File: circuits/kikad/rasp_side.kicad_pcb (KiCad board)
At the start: 2 copper layers, 33 parts, among them J1 RJ45, J2 RJ45, J3 RJ45, J4 RJ45, P1 CONN_13X2

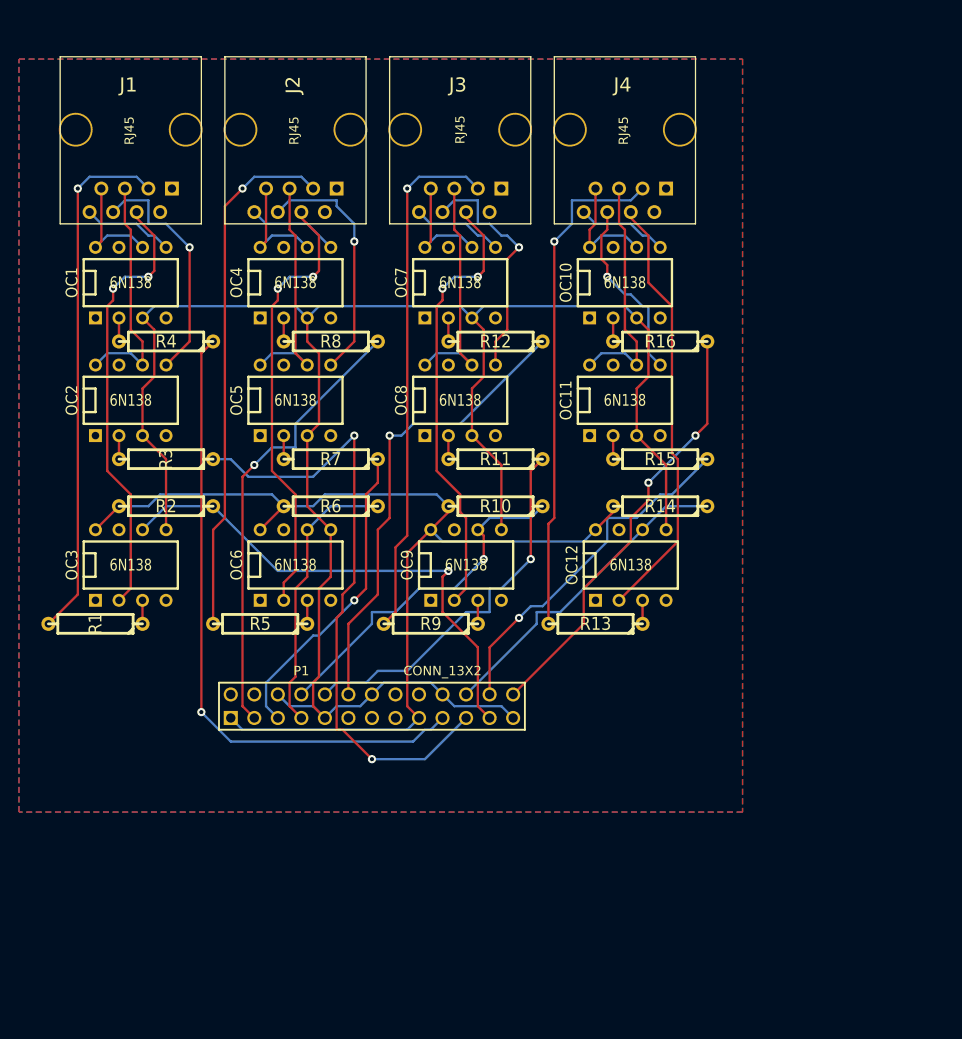
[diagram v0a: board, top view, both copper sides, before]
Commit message: improved version of the kicad circuit
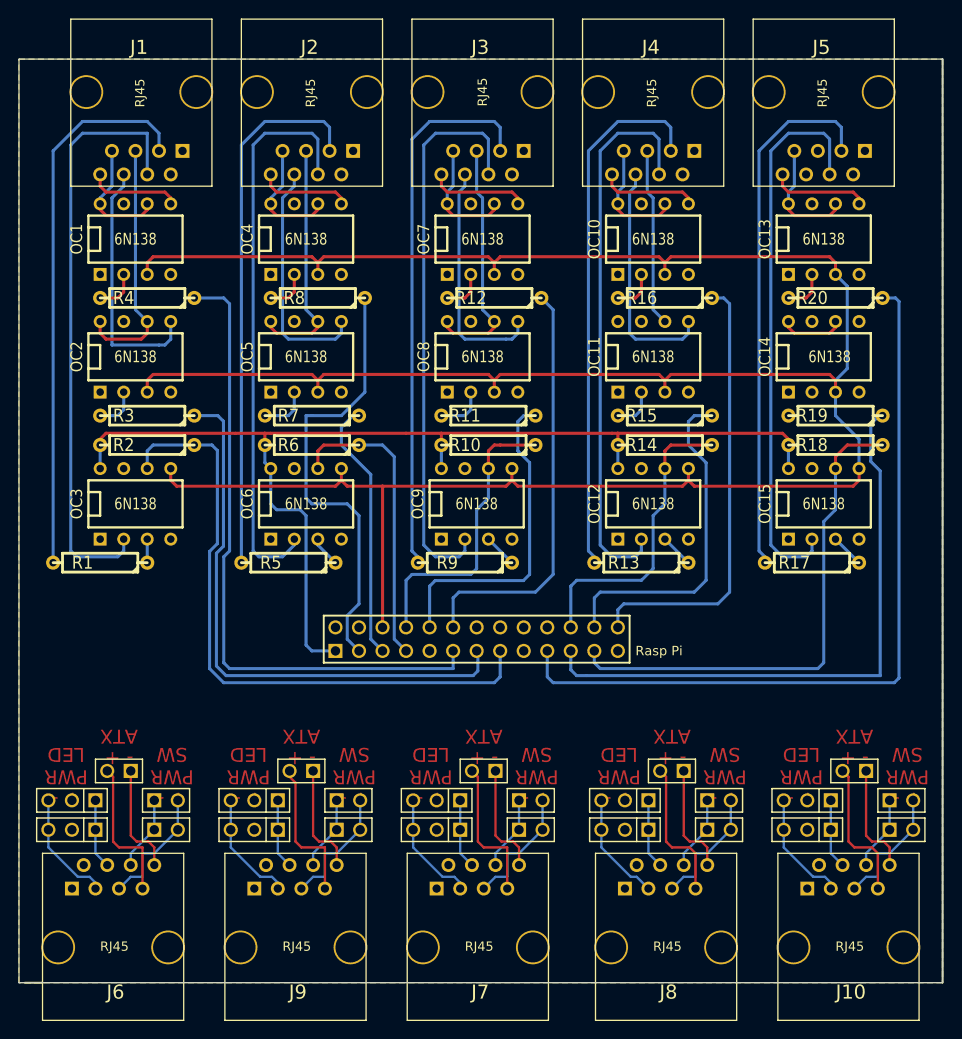
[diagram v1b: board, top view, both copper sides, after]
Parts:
- removed P1: CONN_13X2, pin_array_13x2
- added ?: , PIN_ARRAY_3X1, F.Cu at (95.2, 93.3)
- added ?: , PIN_ARRAY_3X1, F.Cu at (15.9, 90.2)
- added ?: , PIN_ARRAY_2X1, F.Cu at (100.3, 87.0)
- added ?: , PIN_ARRAY_2X1, F.Cu at (105.4, 93.3)
- added ?: , PIN_ARRAY_2X1, F.Cu at (40.6, 87.0)
- added ?: , PIN_ARRAY_2X1, F.Cu at (45.7, 93.3)
- added ?: , PIN_ARRAY_2X1, F.Cu at (45.7, 90.2)
- added ?: , PIN_ARRAY_2X1, F.Cu at (105.4, 90.2)
- added ?: , PIN_ARRAY_2X1, F.Cu at (80.6, 87.0)
- added ?: , PIN_ARRAY_2X1, F.Cu at (85.7, 93.3)
- added ?: , PIN_ARRAY_2X1, F.Cu at (85.7, 90.2)
- added ?: , PIN_ARRAY_3X1, F.Cu at (35.6, 93.3)
- added ?: , PIN_ARRAY_2X1, F.Cu at (60.3, 87.0)
- added ?: , PIN_ARRAY_2X1, F.Cu at (65.4, 93.3)
- added ?: , PIN_ARRAY_2X1, F.Cu at (65.4, 90.2)
- added ?: , PIN_ARRAY_2X1, F.Cu at (21.0, 87.0)
- added ?: , PIN_ARRAY_2X1, F.Cu at (26.0, 90.2)
- added ?: , PIN_ARRAY_2X1, F.Cu at (26.0, 93.3)
- added ?: , PIN_ARRAY_3X1, F.Cu at (35.6, 90.2)
- added ?: , PIN_ARRAY_3X1, F.Cu at (75.6, 93.3)
- added ?: , PIN_ARRAY_3X1, F.Cu at (75.6, 90.2)
- added ?: , PIN_ARRAY_3X1, F.Cu at (95.2, 90.2)
- added ?: , PIN_ARRAY_3X1, F.Cu at (55.2, 93.3)
- added ?: , PIN_ARRAY_3X1, F.Cu at (55.2, 90.2)
- added ?: , PIN_ARRAY_3X1, F.Cu at (15.9, 93.3)
- added J10: RJ45, RJ45_8, F.Cu at (99.7, 106.0)
- added J5: RJ45, RJ45_8, F.Cu at (97.0, 13.7)
- added J6: RJ45, RJ45_8, F.Cu at (20.3, 106.0)
- added J7: RJ45, RJ45_8, F.Cu at (59.7, 106.0)
- added J8: RJ45, RJ45_8, F.Cu at (80.0, 106.0)
- added J9: RJ45, RJ45_8, F.Cu at (40.0, 106.0)
- added OC13: 6N138, DIP-8__300, F.Cu at (97.0, 29.6)
- added OC14: 6N138, DIP-8__300, F.Cu at (97.0, 42.3)
- added OC15: 6N138, DIP-8__300, F.Cu at (97.0, 58.2)
- added R17: 4k, R4, F.Cu at (95.8, 64.5)
- added R18: 10k, R4, F.Cu at (98.3, 51.8)
- added R19: 1.2k, R4, F.Cu at (98.3, 48.6)
- added R20: 1.2k, R4, F.Cu at (98.3, 35.9)
- added Rasp Pi: , pin_array_13x2, F.Cu at (59.6, 72.8)
- moved R13 8.26 mm to (77.3, 64.5)
- moved R9 7.56 mm to (58.3, 64.5)
- moved R5 7.27 mm to (39.2, 64.5)
- moved OC12 7.03 mm to (78.6, 58.2)
- moved R2 6.91 mm to (24.0, 51.8)
- moved R6 6.91 mm to (41.8, 51.8)
- moved OC6 6.70 mm to (41.1, 58.2)
- moved OC9 6.70 mm to (59.6, 58.2)
- moved R10 6.65 mm to (60.8, 51.8)
- moved OC3 6.62 mm to (22.7, 58.2)
- moved R1 6.62 mm to (18.9, 64.5)
- moved R14 6.62 mm to (79.9, 51.8)
- moved OC11 5.60 mm to (78.6, 42.3)
- moved OC10 5.60 mm to (78.6, 29.6)
- moved OC8 5.28 mm to (60.2, 42.3)
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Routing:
- net N-0000020: track 0.00 -> 83.8 mm
- net GND: track 208.1 -> 286.5 mm
- net N-0000021: track 0.00 -> 64.9 mm
- net N-000005: track 0.00 -> 60.3 mm
- net N-000001: track 0.00 -> 57.7 mm
- net N-0000018: track 0.00 -> 54.9 mm
- net N-0000092: track 47.9 -> 64.6 mm, vias 2 -> 0
- net N-0000074: track 0.00 -> 15.8 mm
- net N-0000010: track 0.00 -> 15.8 mm
- net N-0000046: track 0.00 -> 15.8 mm
- net N-0000079: track 0.00 -> 15.4 mm
- net N-0000057: track 0.00 -> 15.4 mm
- net N-0000094: track 55.2 -> 68.9 mm, vias 1 -> 0
- net N-0000066: track 0.00 -> 13.6 mm
- net N-0000082: track 0.00 -> 13.6 mm
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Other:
- board outline added: 99.7 x 99.7 mm
- net class Default: clearance 0.254 -> 0.3302; trace_width 0.254 -> 0.3302
- rule trace_clearance: 0.254 -> 0.3302
- board text added: "+ - PWR LED"
- board text added: "+ - PWR SW"
- board text added: "- + ATX"

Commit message: update the circuit a little
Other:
- board text added: "3.3"
- board text added: "A1"
- board text added: "A2"
- board text added: "A3"
- board text added: "GND"
- board text added: "L1"
- board text added: "L2"
- board text added: "L3"
- board text added: "MùPùF, 2014"
- board text added: "P1"
- board text added: "P2"
- board text added: "P3"
- board text added: "Rasp/Wt-RPM 2014, MùPùF"
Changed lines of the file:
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@@
     (links 151)
     (no_connects 5)
-    (area 10.109999 5.702299 109.955001 114.312701)
+    (area 10.059999 5.448299 109.955001 114.312701)
     (thickness 1.6)
-    (drawings 21)
+    (drawings 60)
     (tracks 599)
     (zones 0)
@@
     )
   )
+  (gr_text A3 (at 57.15 68.326 90) (layer F.SilkS)
+    (effects (font (size 1.5 1.5) (thickness 0.3)))
+  )
+  (gr_text P3 (at 54.61 68.326 90) (layer F.SilkS)
+    (effects (font (size 1.5 1.5) (thickness 0.3)))
+  )
+  (gr_text L3 (at 52.07 68.326 90) (layer F.SilkS)
+    (effects (font (size 1.5 1.5) (thickness 0.3)))
+  )
+  (gr_text L2 (at 52.07 76.962 90) (layer F.SilkS)
+    (effects (font (size 1.5 1.5) (thickness 0.3)))
+  )
+  (gr_text P2 (at 49.53 76.962 90) (layer F.SilkS)
+    (effects (font (size 1.5 1.5) (thickness 0.3)))
+  )
+  (gr_text A2 (at 46.736 76.962 90) (layer F.SilkS)
+    (effects (font (size 1.5 1.5) (thickness 0.3)))
+  )
+  (gr_text L1 (at 62.23 76.708 90) (layer F.SilkS)
+    (effects (font (size 1.5 1.5) (thickness 0.3)))
+  )
+  (gr_text P1 (at 59.69 76.708 90) (layer F.SilkS)
+    (effects (font (size 1.5 1.5) (thickness 0.3)))
+  )
+  (gr_text A1 (at 57.15 76.708 90) (layer F.SilkS)
+    (effects (font (size 1.5 1.5) (thickness 0.3)))
+  )
+  (gr_line (start 89.916 109.728) (end 89.916 80.01) (angle 90) (layer B.SilkS) (width 0.2))
+  (gr_line (start 69.85 109.728) (end 69.85 80.01) (angle 90) (layer B.SilkS) (width 0.2))
+  (gr_line (start 50.038 80.01) (end 50.292 80.264) (angle 90) (layer B.SilkS) (width 0.2))
+  (gr_line (start 50.038 109.982) (end 50.038 80.01) (angle 90) (layer B.SilkS) (width 0.2))
+  (gr_line (start 30.226 80.01) (end 30.226 108.458) (angle 90) (layer B.SilkS) (width 0.2))
+  (gr_line (start 30.226 109.728) (end 30.226 80.01) (angle 90) (layer B.SilkS) (width 0.2))
+  (gr_text "MùPùF, 2014" (at 100.076 83.566 180) (layer B.SilkS)
+    (effects (font (size 1.5 1.5) (thickness 0.3)) (justify mirror))
+  )
+  (gr_text "MùPùF, 2014" (at 80.518 83.566 180) (layer B.SilkS)
+    (effects (font (size 1.5 1.5) (thickness 0.3)) (justify mirror))
+  )
+  (gr_text "MùPùF, 2014" (at 60.198 83.82 180) (layer B.SilkS)
+    (effects (font (size 1.5 1.5) (thickness 0.3)) (justify mirror))
+  )
+  (gr_text "MùPùF, 2014" (at 40.64 83.82 180) (layer B.SilkS)
+    (effects (font (size 1.5 1.5) (thickness 0.3)) (justify mirror))
+  )
+  (gr_text "- +\nATX" (at 20.955 84.455 180) (layer F.Cu)
+    (effects (font (size 1.5 1.5) (thickness 0.3)))
+  )
+  (gr_text "MùPùF, 2014" (at 21.082 83.82 180) (layer B.SilkS)
+    (effects (font (size 1.5 1.5) (thickness 0.3)) (justify mirror))
+  )
+  (gr_text "MùPùF, 2014" (at 21.082 83.82 180) (layer B.SilkS)
+    (effects (font (size 1.5 1.5) (thickness 0.3)) (justify mirror))
+  )
+  (gr_text "- +\nATX" (at 20.955 84.455 180) (layer F.Cu)
+    (effects (font (size 1.5 1.5) (thickness 0.3)))
+  )
+  (gr_text "- +\nATX" (at 20.955 84.455 180) (layer F.Cu)
+    (effects (font (size 1.5 1.5) (thickness 0.3)))
+  )
+  (gr_text "MùPùF, 2014" (at 21.082 83.82 180) (layer B.SilkS)
+    (effects (font (size 1.5 1.5) (thickness 0.3)) (justify mirror))
+  )
+  (gr_text "MùPùF, 2014" (at 21.082 83.82 180) (layer B.SilkS)
+    (effects (font (size 1.5 1.5) (thickness 0.3)) (justify mirror))
+  )
+  (gr_text "Rasp/Wt-RPM\n\n2014, MùPùF" (at 19.812 71.374) (layer F.SilkS)
+    (effects (font (size 1.5 1.5) (thickness 0.3)))
+  )
+  (gr_text GND (at 49.53 67.564 90) (layer F.SilkS)
+    (effects (font (size 1.5 1.5) (thickness 0.3)))
+  )
+  (gr_text 3.3 (at 44.45 77.216 90) (layer F.SilkS)
+    (effects (font (size 1.5 1.5) (thickness 0.3)))
+  )
+  (gr_line (start 10.668 80.01) (end 109.728 80.01) (angle 90) (layer F.SilkS) (width 0.2))
+  (gr_line (start 89.916 80.01) (end 89.916 109.728) (angle 90) (layer F.Paste) (width 0.2))
+  (gr_line (start 69.85 109.728) (end 69.85 108.712) (angle 90) (layer F.Paste) (width 0.2))
+  (gr_line (start 69.85 80.01) (end 69.85 109.728) (angle 90) (layer F.Paste) (width 0.2))
+  (gr_line (start 50.038 80.01) (end 50.038 109.728) (angle 90) (layer F.Paste) (width 0.2))
+  (gr_line (start 30.226 80.264) (end 30.226 109.982) (angle 90) (layer F.Paste) (width 0.2))
+  (gr_line (start 30.48 109.728) (end 30.48 109.474) (angle 90) (layer F.Paste) (width 0.2))
+  (gr_line (start 10.16 80.01) (end 11.938 80.01) (angle 90) (layer F.Paste) (width 0.2))
+  (gr_line (start 109.474 80.01) (end 109.728 80.01) (angle 90) (layer F.Paste) (width 0.2))
+  (gr_line (start 11.938 80.01) (end 109.474 80.01) (angle 90) (layer F.Paste) (width 0.2))
   (gr_text "- +\nATX" (at 100.33 84.455 180) (layer F.Cu)
     (effects (font (size 1.5 1.5) (thickness 0.3)))
@@
     (effects (font (size 1.5 1.5) (thickness 0.3)))
   )
-  (gr_text "+ -\nPWR\nSW" (at 26.67 87.63 180) (layer F.Cu)
+  (gr_text "+ -\nPWR\nSW" (at 26.162 88.138 180) (layer F.Cu)
     (effects (font (size 1.5 1.5) (thickness 0.3)))
   )

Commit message: kicad: add holes in the circuit
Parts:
- added ?: , 1pin, F.Cu at (15.2, 74.4)
- added ?: , 1pin, F.Cu at (104.6, 75.9)
- added ?: , 1pin, F.Cu at (105.9, 29.7)
- added ?: , small_hole, F.Cu at (13.0, 81.5)
- added ?: , small_hole, F.Cu at (27.9, 81.5)
- added ?: , small_hole, F.Cu at (32.5, 81.5)
- added ?: , small_hole, F.Cu at (48.0, 81.5)
- added ?: , small_hole, F.Cu at (52.3, 81.5)
- added ?: , small_hole, F.Cu at (68.1, 81.5)
- added ?: , small_hole, F.Cu at (72.6, 81.5)
- added ?: , small_hole, F.Cu at (88.1, 81.5)
- added ?: , small_hole, F.Cu at (92.7, 81.5)
- added ?: , small_hole, F.Cu at (107.4, 81.5)
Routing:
- net N-000003: track 0.00 -> 25.6 mm
- net +3.3V: track 118.4 -> 140.8 mm
- net N-000004: track 6.88 -> 26.1 mm
- net N-0000032: track 19.2 -> 25.4 mm
- net GND: track 286.5 -> 291.9 mm
- net N-000008: track 0.00 -> 4.48 mm
- net N-0000021: track 64.9 -> 63.2 mm
- net N-0000018: track 54.9 -> 53.4 mm
- net N-0000020: track 83.8 -> 83.0 mm
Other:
- board text added: "A4"
- board text added: "A5"
- board text added: "L = PW LED P = PW SW A = ATX SW"
- board text added: "L4"
- board text added: "L5"
- board text added: "P4"
- board text added: "P5"
- board text added: "Wt-RPM 2014, MùPùF"
- board text removed: "Rasp/Wt-RPM 2014, MùPùF"

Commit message: kicad: style fixes
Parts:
- moved ? 0.25 mm to (13.0, 81.8)
- moved ? 0.25 mm to (27.9, 81.8)
- moved ? 0.25 mm to (32.5, 81.8)
- moved ? 0.25 mm to (48.0, 81.8)
- moved ? 0.25 mm to (52.3, 81.8)
- moved ? 0.25 mm to (68.1, 81.8)
- moved ? 0.25 mm to (72.6, 81.8)
- moved ? 0.25 mm to (88.1, 81.8)
- moved ? 0.25 mm to (92.7, 81.8)
- moved ? 0.25 mm to (107.4, 81.8)
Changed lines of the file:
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@@
     (area 10.059999 5.448299 109.955001 114.312701)
     (thickness 1.6)
-    (drawings 74)
+    (drawings 67)
     (tracks 638)
     (zones 0)
@@
   )
   (module small_hole (layer F.Cu)
-    (at 12.954 81.534)
+    (at 12.954 81.788)
     (descr "module 1 pin (ou trou mecanique de percage)")
     (tags DEV)
@@
   )
   (module small_hole (layer F.Cu)
-    (at 27.94 81.534)
+    (at 27.94 81.788)
     (descr "module 1 pin (ou trou mecanique de percage)")
     (tags DEV)
@@
   )
   (module small_hole (layer F.Cu)
-    (at 32.512 81.534)
+    (at 32.512 81.788)
     (descr "module 1 pin (ou trou mecanique de percage)")
     (tags DEV)
@@
   )
   (module small_hole (layer F.Cu)
-    (at 48.006 81.534)
+    (at 48.006 81.788)
     (descr "module 1 pin (ou trou mecanique de percage)")
     (tags DEV)
@@
   )
   (module small_hole (layer F.Cu)
-    (at 52.324 81.534)
+    (at 52.324 81.788)
     (descr "module 1 pin (ou trou mecanique de percage)")
     (tags DEV)
@@
   )
   (module small_hole (layer F.Cu)
-    (at 68.072 81.534)
+    (at 68.072 81.788)
     (descr "module 1 pin (ou trou mecanique de percage)")
     (tags DEV)
@@
   )
   (module small_hole (layer F.Cu)
-    (at 72.644 81.534)
+    (at 72.644 81.788)
     (descr "module 1 pin (ou trou mecanique de percage)")
     (tags DEV)
@@
   )
   (module small_hole (layer F.Cu)
-    (at 88.138 81.534)
+    (at 88.138 81.788)
     (descr "module 1 pin (ou trou mecanique de percage)")
     (tags DEV)
@@
   )
   (module small_hole (layer F.Cu)
-    (at 92.71 81.534)
+    (at 92.71 81.788)
     (descr "module 1 pin (ou trou mecanique de percage)")
     (tags DEV)
@@
   )
   (module small_hole (layer F.Cu)
-    (at 107.442 81.534)
+    (at 107.442 81.788)
     (descr "module 1 pin (ou trou mecanique de percage)")
     (tags DEV)
@@
     )
   )
+  (gr_text "MùPùF, 2014" (at 20.828 84.074 180) (layer B.SilkS)
+    (effects (font (size 1.5 1.5) (thickness 0.3)) (justify mirror))
+  )
   (gr_line (start 90.424 80.264) (end 90.424 79.502) (angle 90) (layer F.SilkS) (width 0.2))
   (gr_line (start 50.292 80.01) (end 50.292 79.502) (angle 90) (layer F.SilkS) (width 0.2))
@@
   )
   (gr_line (start 30.226 80.264) (end 30.226 109.982) (angle 90) (layer F.Paste) (width 0.2))
-  (gr_text "MùPùF, 2014" (at 21.082 83.82 180) (layer B.SilkS)
-    (effects (font (size 1.5 1.5) (thickness 0.3)) (justify mirror))
-  )
-  (gr_text "MùPùF, 2014" (at 21.082 83.82 180) (layer B.SilkS)
-    (effects (font (size 1.5 1.5) (thickness 0.3)) (justify mirror))
-  )
-  (gr_text "MùPùF, 2014" (at 21.082 83.82 180) (layer B.SilkS)
-    (effects (font (size 1.5 1.5) (thickness 0.3)) (justify mirror))
-  )
-  (gr_text "MùPùF, 2014" (at 21.082 83.82 180) (layer B.SilkS)
-    (effects (font (size 1.5 1.5) (thickness 0.3)) (justify mirror))
-  )
   (gr_line (start 30.226 109.728) (end 30.226 80.01) (angle 90) (layer B.SilkS) (width 0.2))
   (gr_line (start 30.226 80.01) (end 30.226 108.458) (angle 90) (layer B.SilkS) (width 0.2))
@@
   (gr_line (start 30.226 80.01) (end 30.226 108.458) (angle 90) (layer B.SilkS) (width 0.2))
   (gr_line (start 30.226 109.728) (end 30.226 80.01) (angle 90) (layer B.SilkS) (width 0.2))
-  (gr_text "MùPùF, 2014" (at 100.076 83.566 180) (layer B.SilkS)
+  (gr_text "MùPùF, 2014" (at 100.076 84.074 180) (layer B.SilkS)
     (effects (font (size 1.5 1.5) (thickness 0.3)) (justify mirror))
   )
-  (gr_text "MùPùF, 2014" (at 80.518 83.566 180) (layer B.SilkS)
+  (gr_text "MùPùF, 2014" (at 80.264 83.82 180) (layer B.SilkS)
     (effects (font (size 1.5 1.5) (thickness 0.3)) (justify mirror))
   )
@@
     (effects (font (size 1.5 1.5) (thickness 0.3)) (justify mirror))
   )
-  (gr_text "MùPùF, 2014" (at 40.64 83.82 180) (layer B.SilkS)
-    (effects (font (size 1.5 1.5) (thickness 0.3)) (justify mirror))
-  )
-  (gr_text "MùPùF, 2014" (at 21.082 83.82 180) (layer B.SilkS)
-    (effects (font (size 1.5 1.5) (thickness 0.3)) (justify mirror))
-  )
-  (gr_text "MùPùF, 2014" (at 21.082 83.82 180) (layer B.SilkS)
-    (effects (font (size 1.5 1.5) (thickness 0.3)) (justify mirror))
-  )
-  (gr_text "MùPùF, 2014" (at 21.082 83.82 180) (layer B.SilkS)
-    (effects (font (size 1.5 1.5) (thickness 0.3)) (justify mirror))
-  )
-  (gr_text "MùPùF, 2014" (at 21.082 83.82 180) (layer B.SilkS)
+  (gr_text "MùPùF, 2014" (at 40.132 84.074 180) (layer B.SilkS)
     (effects (font (size 1.5 1.5) (thickness 0.3)) (justify mirror))
   )
